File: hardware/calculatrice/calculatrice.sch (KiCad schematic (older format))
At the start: 57 parts, among them J1 Conn_01x02_Male, J2 Conn_01x06_MountingPin, J4 Conn_01x01, J5 Conn_01x01, J6 Conn_01x01, J7 Conn_01x01, J8 Conn_01x01, SW1 SW_ON, SW10 SW_Push_45deg, SW11 SW_Push_45deg, SW12 SW_Push_45deg, SW13 SW_Push_45deg, SW14 SW_Push_45deg, SW15 SW_Push_45deg, SW16 SW_Push_45deg, SW17 SW_Push_45deg, SW18 SW_Push_45deg, SW19 SW_Push_45deg, SW2 SW_Push_45deg, SW20 SW_Push_45deg, SW21 SW_Push_45deg, SW22 SW_Push_45deg, SW23 SW_Push_45deg, SW24 SW_Push_45deg, SW25 SW_Push_45deg, SW26 SW_Push_45deg, SW27 SW_Push_45deg, SW28 SW_Push_45deg, SW29 SW_Push_45deg, SW3 SW_Push_45deg, SW30 SW_Push_45deg, SW31 SW_Push_45deg, SW32 SW_Push_45deg, SW33 SW_Push_45deg, SW34 SW_Push_45deg, SW35 SW_Push_45deg, SW36 SW_Push_45deg, SW4 SW_Push_45deg, SW5 SW_Push_45deg, SW6 SW_Push_45deg, SW7 SW_Push_45deg, SW8 SW_Push_45deg, SW9 SW_Push_45deg, U1 24LC64, U2 pic24FJ64GA002, U3 LCD-016N002L

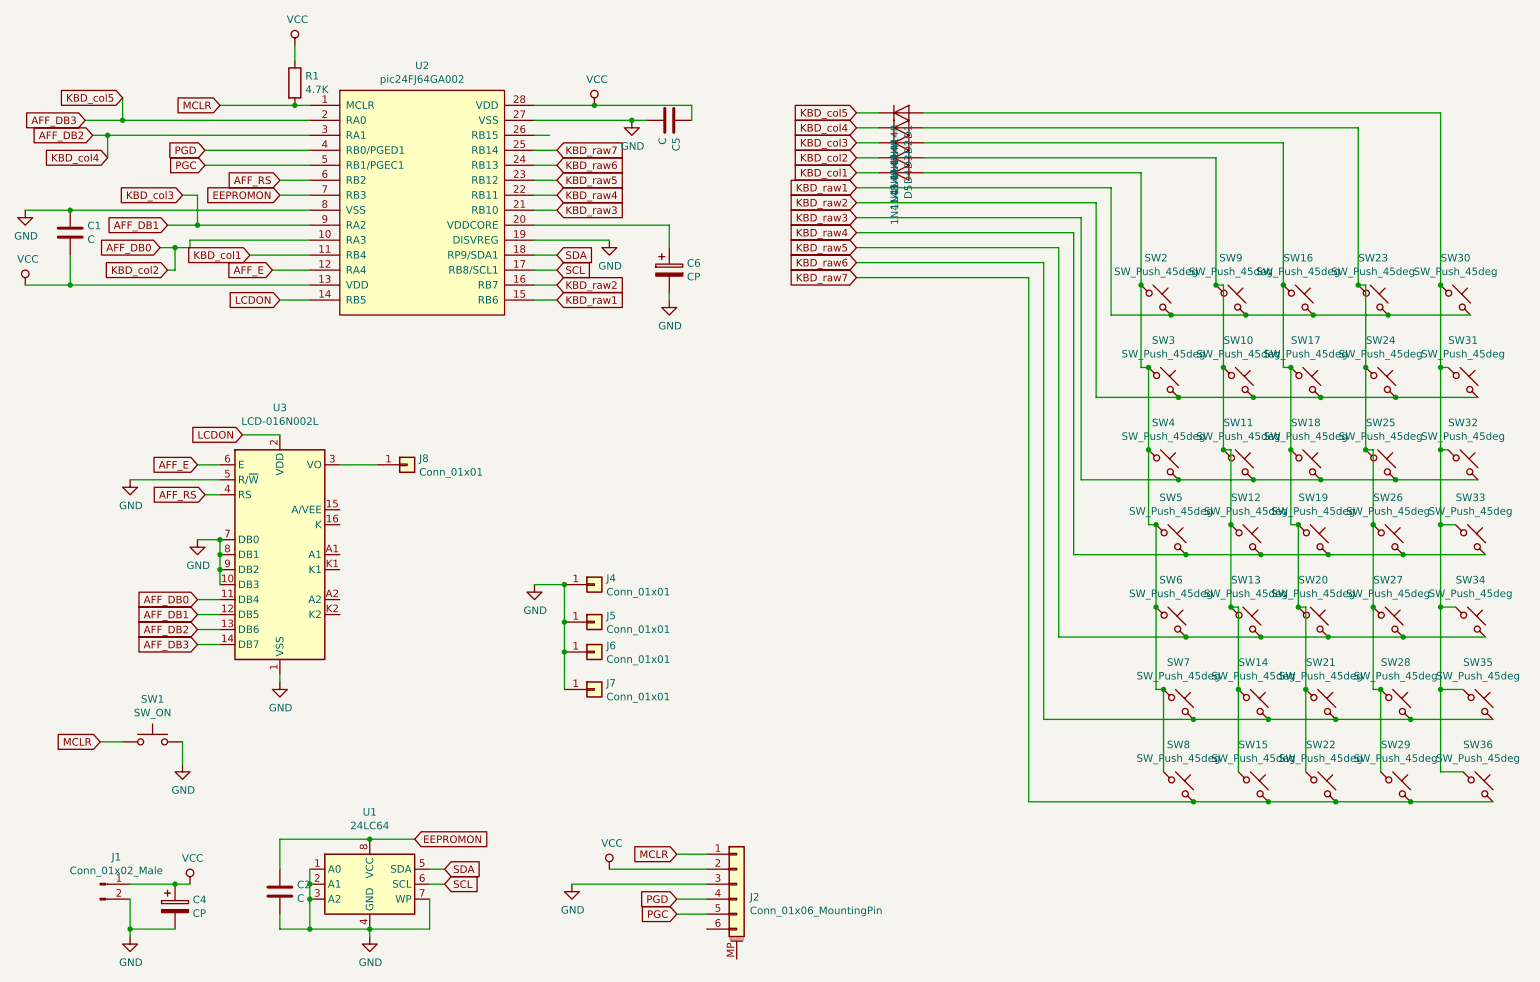
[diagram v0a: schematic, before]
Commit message: Developpement
RPN Calculator protptype
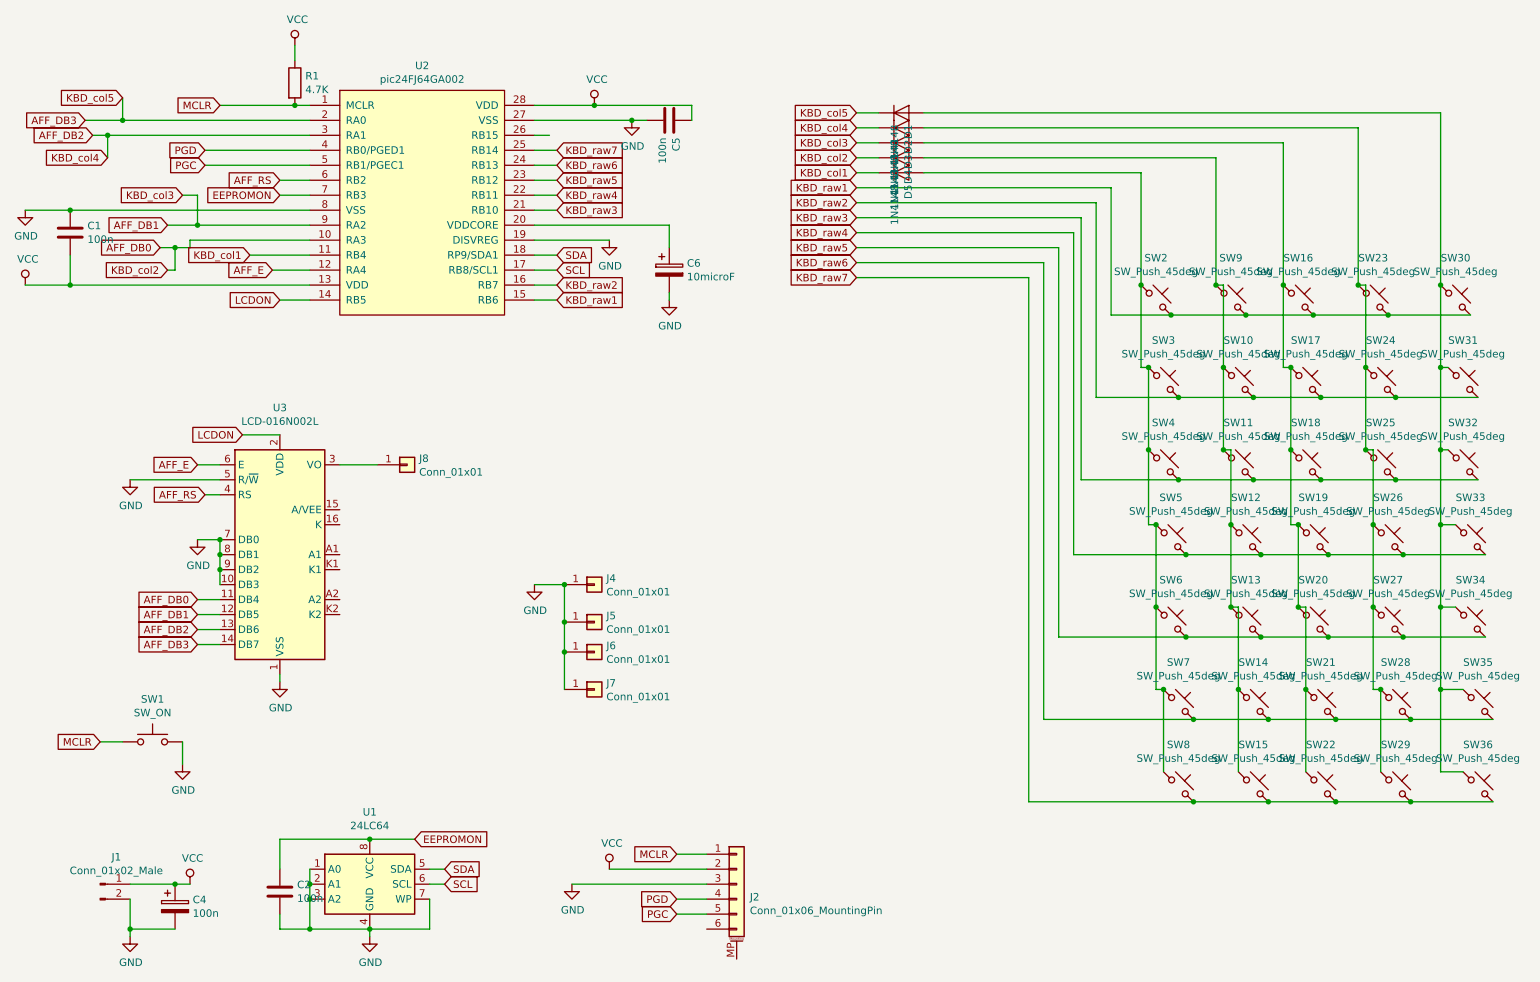
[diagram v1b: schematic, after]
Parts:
- C1, C2, C5: value C -> 100n
- C4: value CP -> 100n
- C6: value CP -> 10microF
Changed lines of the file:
@@
 P 1600 7000
 F 0 "C4" H 1718 7046 50  0000 L CNN
-F 1 "CP" H 1718 6955 50  0000 L CNN
+F 1 "100n" H 1718 6955 50  0000 L CNN
 F 2 "Capacitors_ThroughHole:C_Rect_L4_W2.5_P2.5" H 1638 6850 50  0001 C CNN
 F 3 "~" H 1600 7000 50  0001 C CNN
@@
 P 900 2500
 F 0 "C1" H 1015 2546 50  0000 L CNN
-F 1 "C" H 1015 2455 50  0000 L CNN
+F 1 "100n" H 1015 2455 50  0000 L CNN
 F 2 "Capacitors_ThroughHole:C_Rect_L4_W2.5_P2.5" H 938 2350 50  0001 C CNN
 F 3 "~" H 900 2500 50  0001 C CNN
@@
 P 4900 2750
 F 0 "C6" H 5018 2796 50  0000 L CNN
-F 1 "CP" H 5018 2705 50  0000 L CNN
+F 1 "10microF" H 5018 2705 50  0000 L CNN
 F 2 "Capacitors_ThroughHole:C_Radial_D5_L6_P2.5" H 4938 2600 50  0001 C CNN
 F 3 "~" H 4900 2750 50  0001 C CNN
@@
 P 4900 1750
 F 0 "C5" H 5015 1796 50  0000 L CNN
-F 1 "C" H 5015 1705 50  0000 L CNN
+F 1 "100n" H 5015 1705 50  0000 L CNN
 F 2 "Capacitors_ThroughHole:C_Rect_L4_W2.5_P2.5" H 4938 1600 50  0001 C CNN
 F 3 "~" H 4900 1750 50  0001 C CNN
@@
 P 2300 6900
 F 0 "C2" H 2415 6946 50  0000 L CNN
-F 1 "C" H 2415 6855 50  0000 L CNN
+F 1 "100n" H 2415 6855 50  0000 L CNN
 F 2 "Capacitors_ThroughHole:C_Rect_L4_W2.5_P2.5" H 2338 6750 50  0001 C CNN
 F 3 "~" H 2300 6900 50  0001 C CNN
